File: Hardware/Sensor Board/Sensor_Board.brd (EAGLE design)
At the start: 100 x 80 mm, 19 parts, among them Q1 MOSFET-NCHANNELFQP30N06L, U1 ATMEGA328P_PDIP

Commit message: Add communications
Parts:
- added FRAME1: FRAME-LETTER, SparkFun-Aesthetics:CREATIVE_COMMONS
- added R1, R3: 120, SparkFun-Passives:1206
- added U$7: MAX3077, MAX3077:MAX3070E
- added U$8: RJ45-8PTH, SparkFun-Connectors:RJ45-8
- C1: device SparkFun-Capacitors:1206 -> SparkFun-Capacitors:CPOL-RADIAL-100UF-25V
- C5: value 100uF -> 10uF
- moved U$2 75.7 mm to (-22.9, -174.0)
- moved C1 56.2 mm to (-24.1, -100.3)
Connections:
- new net N$6: R1.1, U$7.A, U$8.1
- new net N$7: R1.2, U$7.B, U$8.2
- new net N$8: R3.1, U$7.Z, U$8.6
- new net N$9: R3.2, U$7.Y, U$8.3
- new net ROVECOMM_RX: U$7.RO, U1.2
- new net ROVECOMM_TX: U$7.DI, U1.3
- net 5V: now also U$7.VCC
- net GND: now also U$7.GND
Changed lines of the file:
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@@
 <element name="12V_INPUT" library="SparkFun-Connectors" package="MOLEX-1X2" value="M02POLAR" x="-7.62" y="-21.59"/>
 <element name="R2" library="SparkFun-Passives" package="1206" value="1k" x="-6.35" y="-35.56"/>
-<element name="C5" library="SparkFun-Capacitors" package="1206" value="100uF" x="-6.35" y="-39.37"/>
+<element name="C5" library="SparkFun-Capacitors" package="1206" value="10uF" x="-6.35" y="-39.37"/>
 <element name="C6" library="SparkFun-Capacitors" package="1206" value="10uF" x="-6.35" y="-43.18"/>
-<element name="C1" library="SparkFun-Capacitors" package="1206" value="100uF" x="-6.35" y="-46.99"/>
 <element name="LED1" library="SparkFun-LED" package="LED-1206" value="" x="-6.35" y="-52.07"/>
 <element name="U$1" library="MRDT-2015-PowerBoard" package="OKI-78SRH" value="Q_OKI-78SR" x="-15.24" y="-49.53"/>
-<element name="U$2" library="MRDT-2015-General" package="TEST" value="TEST" x="6.35" y="-104.14"/>
+<element name="C1" library="SparkFun-Capacitors" package="CPOL-RADIAL-100UF-25V" value="100uF" x="-24.13" y="-100.33"/>
+<element name="U$7" library="MAX3077" package="MAX3070E" value="MAX3077" x="-30.48" y="-100.33"/>
+<element name="U$8" library="SparkFun-Connectors" package="RJ45-8" value="RJ45-8PTH" x="-41.91" y="-93.98"/>
+<element name="R1" library="SparkFun-Passives" package="1206" value="120" x="-46.99" y="-107.95"/>
+<element name="R3" library="SparkFun-Passives" package="1206" value="120" x="-46.99" y="-111.76"/>
+<element name="FRAME1" library="SparkFun-Aesthetics" package="CREATIVE_COMMONS" value="FRAME-LETTER" x="-27.94" y="-121.92"/>
+<element name="U$2" library="MRDT-2015-General" package="TEST" value="TEST" x="-22.86" y="-173.99"/>
 </elements>
 <signals>
@@
 <contactref element="U$4" pad="GND"/>
 <contactref element="Q1" pad="3"/>
+<contactref element="U$1" pad="2"/>
 <contactref element="C1" pad="2"/>
-<contactref element="U$1" pad="2"/>
-<wire x1="33.02" y1="44.45" x2="30.61" y2="46.99" width="0" layer="19" extent="1-1"/>
+<contactref element="U$7" pad="GND"/>
+<wire x1="-25.4" y1="-100.33" x2="-28.575" y2="-103.1875" width="0" layer="19" extent="1-1"/>
+<wire x1="-15.24" y1="-49.53" x2="-25.4" y2="-100.33" width="0" layer="19" extent="1-1"/>
+<wire x1="-4.95" y1="-43.18" x2="-15.24" y2="-49.53" width="0" layer="19" extent="1-1"/>
+<wire x1="-4.95" y1="-39.37" x2="-4.95" y2="-43.18" width="0" layer="19" extent="1-1"/>
+<wire x1="-4.95" y1="-35.56" x2="-4.95" y2="-39.37" width="0" layer="19" extent="1-1"/>
+<wire x1="-7.62" y1="-21.59" x2="-4.95" y2="-35.56" width="0" layer="19" extent="1-1"/>
+<wire x1="7.62" y1="-19.05" x2="-7.62" y2="-21.59" width="0" layer="19" extent="1-1"/>
+<wire x1="5.08" y1="-10.16" x2="7.62" y2="-19.05" width="0" layer="19" extent="1-1"/>
+<wire x1="49.53" y1="10.16" x2="5.08" y2="-10.16" width="0" layer="19" extent="1-1"/>
+<wire x1="30.61" y1="46.99" x2="33.02" y2="44.45" width="0" layer="19" extent="1-1"/>
 <wire x1="21.46" y1="46.99" x2="30.61" y2="46.99" width="0" layer="19" extent="1-1"/>
-<wire x1="5.08" y1="-10.16" x2="49.53" y2="10.16" width="0" layer="19" extent="1-1"/>
-<wire x1="7.62" y1="-19.05" x2="5.08" y2="-10.16" width="0" layer="19" extent="1-1"/>
-<wire x1="-7.62" y1="-21.59" x2="7.62" y2="-19.05" width="0" layer="19" extent="1-1"/>
-<wire x1="-4.95" y1="-35.56" x2="-7.62" y2="-21.59" width="0" layer="19" extent="1-1"/>
-<wire x1="-4.95" y1="-39.37" x2="-4.95" y2="-35.56" width="0" layer="19" extent="1-1"/>
-<wire x1="-4.95" y1="-43.18" x2="-4.95" y2="-39.37" width="0" layer="19" extent="1-1"/>
-<wire x1="-4.95" y1="-46.99" x2="-4.95" y2="-43.18" width="0" layer="19" extent="1-1"/>
-<wire x1="-15.24" y1="-49.53" x2="-4.95" y2="-46.99" width="0" layer="19" extent="1-1"/>
 </signal>
 <signal name="5V">
@@
 <contactref element="U$4" pad="VCC"/>
 <contactref element="LED1" pad="A"/>
+<contactref element="U$7" pad="VCC"/>
+<wire x1="-7.85" y1="-52.07" x2="-32.385" y2="-103.1875" width="0" layer="19" extent="1-1"/>
 <wire x1="-7.75" y1="-43.18" x2="-7.85" y2="-52.07" width="0" layer="19" extent="1-1"/>
 <wire x1="10.16" y1="-19.05" x2="-7.75" y2="-43.18" width="0" layer="19" extent="1-1"/>
@@
 <signal name="3V3_LASER">
 <contactref element="JP3" pad="2"/>
+<contactref element="U$1" pad="3"/>
 <contactref element="C1" pad="1"/>
-<contactref element="U$1" pad="3"/>
-<wire x1="-7.75" y1="-46.99" x2="-17.78" y2="-49.53" width="0" layer="19" extent="1-1"/>
-<wire x1="13.97" y1="49.53" x2="-7.75" y2="-46.99" width="0" layer="19" extent="1-1"/>
+<wire x1="-17.78" y1="-49.53" x2="-22.86" y2="-100.33" width="0" layer="19" extent="1-1"/>
+<wire x1="13.97" y1="49.53" x2="-17.78" y2="-49.53" width="0" layer="19" extent="1-1"/>
 </signal>
 <signal name="N$2">
@@
 <wire x1="-7.75" y1="-35.56" x2="-4.85" y2="-52.07" width="0" layer="19" extent="1-1"/>
 </signal>
+<signal name="N$6">
+<contactref element="U$7" pad="A"/>
+<contactref element="R1" pad="1"/>
+<contactref element="U$8" pad="1"/>
+<wire x1="-32.385" y1="-97.4725" x2="-48.39" y2="-107.95" width="0" layer="19" extent="1-1"/>
+<wire x1="-46.355" y1="-87.63" x2="-32.385" y2="-97.4725" width="0" layer="19" extent="1-1"/>
+</signal>
+<signal name="N$7">
+<contactref element="U$7" pad="B"/>
+<contactref element="U$8" pad="2"/>
+<contactref element="R1" pad="2"/>
+<wire x1="-31.115" y1="-97.4725" x2="-45.59" y2="-107.95" width="0" layer="19" extent="1-1"/>
+<wire x1="-45.085" y1="-85.09" x2="-31.115" y2="-97.4725" width="0" layer="19" extent="1-1"/>
+</signal>
+<signal name="N$8">
+<contactref element="U$7" pad="Z"/>
+<contactref element="U$8" pad="6"/>
+<contactref element="R3" pad="1"/>
+<wire x1="-29.845" y1="-97.4725" x2="-48.39" y2="-111.76" width="0" layer="19" extent="1-1"/>
+<wire x1="-40.005" y1="-85.09" x2="-29.845" y2="-97.4725" width="0" layer="19" extent="1-1"/>
+</signal>
+<signal name="N$9">
+<contactref element="U$7" pad="Y"/>
+<contactref element="U$8" pad="3"/>
+<contactref element="R3" pad="2"/>
+<wire x1="-28.575" y1="-97.4725" x2="-45.59" y2="-111.76" width="0" layer="19" extent="1-1"/>
+<wire x1="-43.815" y1="-87.63" x2="-28.575" y2="-97.4725" width="0" layer="19" extent="1-1"/>
+</signal>
+<signal name="ROVECOMM_TX">
+<contactref element="U1" pad="3"/>
+<contactref element="U$7" pad="DI"/>
+<wire x1="45.72" y1="44.45" x2="-29.845" y2="-103.1875" width="0" layer="19" extent="1-1"/>
+</signal>
+<signal name="ROVECOMM_RX">
+<contactref element="U1" pad="2"/>
+<contactref element="U$7" pad="RO"/>
+<wire x1="48.26" y1="44.45" x2="-31.115" y2="-103.1875" width="0" layer="19" extent="1-1"/>
+</signal>
 </signals>

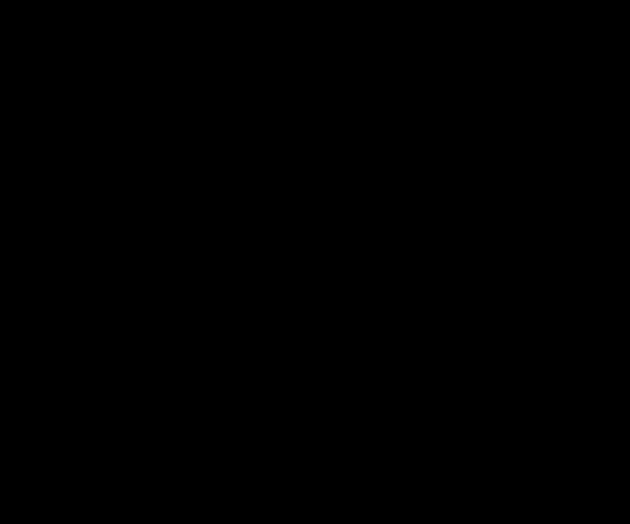
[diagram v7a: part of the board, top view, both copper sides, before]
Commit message: #2 Add reset button to microcontroller
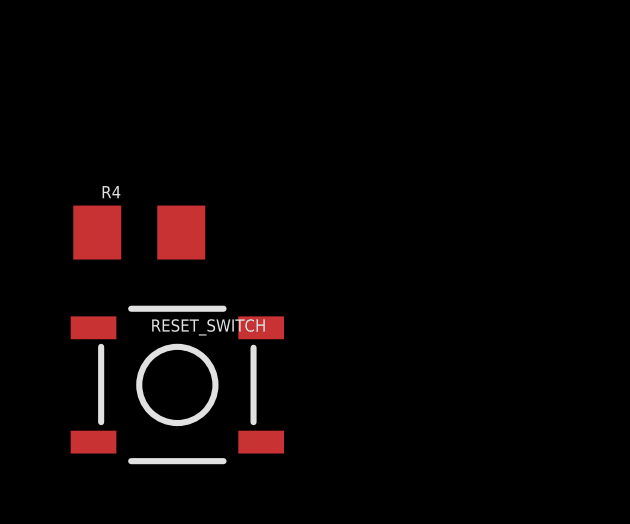
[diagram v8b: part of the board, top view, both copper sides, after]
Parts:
- added R4: 10k, SparkFun-Passives:1206
- added RESET_SWITCH: SWITCH-MOMENTARY-2SMD, SparkFun-Electromechanical:TACTILE-SWITCH-SMD
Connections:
- new net N$10: R4.2, RESET_SWITCH.1, U1.1
- net 3.3V: now also R4.1
- net GND: now also C3.1, C4.1, RESET_SWITCH.3; no longer C3.2, C4.2
- net N$2: now also C4.2; no longer C3.1
- net N$4: now also C3.2; no longer C4.1
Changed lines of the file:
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@@
 <?xml version="1.0" encoding="utf-8"?>
 <!DOCTYPE eagle SYSTEM "eagle.dtd">
-<eagle version="6.5.0">
+<eagle version="7.2.0">
 <drawing>
 <settings>
@@
 <layer number="59" name="tCarbon" color="7" fill="1" visible="no" active="no"/>
 <layer number="60" name="bCarbon" color="7" fill="1" visible="no" active="no"/>
-<layer number="90" name="Modules" color="5" fill="1" visible="yes" active="yes"/>
+<layer number="90" name="Modules" color="5" fill="1" visible="no" active="no"/>
 <layer number="91" name="Nets" color="2" fill="1" visible="no" active="no"/>
 <layer number="92" name="Busses" color="1" fill="1" visible="no" active="no"/>
@@
 <pass name="Default">
 <param name="RoutingGrid" value="50mil"/>
+<param name="AutoGrid" value="1"/>
+<param name="Efforts" value="0"/>
+<param name="TopRouterVariant" value="1"/>
 <param name="tpViaShape" value="round"/>
 <param name="PrefDir.1" value="|"/>
@@
 <element name="FRAME1" library="SparkFun-Aesthetics" package="CREATIVE_COMMONS" value="FRAME-LETTER" x="-27.94" y="-121.92"/>
 <element name="U$2" library="MRDT-2015-General" package="TEST" value="TEST" x="-22.86" y="-173.99"/>
+<element name="R4" library="SparkFun-Passives" package="1206" value="10k" x="-46.99" y="-182.88"/>
+<element name="RESET_SWITCH" library="SparkFun-Electromechanical" package="TACTILE-SWITCH-SMD" value="SWITCH-MOMENTARY-2SMD" x="-45.72" y="-187.96">
+<attribute name="PROD_ID" value="SWCH-08247" x="-45.72" y="-187.96" size="1.778" layer="27" display="off"/>
+</element>
 </elements>
 <signals>
 <signal name="GND">
 <contactref element="U$3" pad="GND"/>
-<contactref element="U1" pad="22"/>
-<contactref element="U1" pad="8"/>
 <contactref element="U$5" pad="GND"/>
 <polygon width="0.4064" layer="16">
@@
 <vertex x="-2.54" y="-3.81"/>
 </polygon>
-<contactref element="C4" pad="2"/>
-<contactref element="C3" pad="2"/>
 <contactref element="U$6" pad="GND"/>
 <contactref element="LM7805" pad="GND"/>
@@
 <contactref element="C1" pad="2"/>
 <contactref element="U$7" pad="GND"/>
+<contactref element="U1" pad="22"/>
+<contactref element="U1" pad="8"/>
+<contactref element="C3" pad="1"/>
+<contactref element="C4" pad="1"/>
+<contactref element="RESET_SWITCH" pad="3"/>
+<wire x1="-28.575" y1="-103.1875" x2="-48.514" y2="-189.865" width="0" layer="19" extent="1-1"/>
 <wire x1="-25.4" y1="-100.33" x2="-28.575" y2="-103.1875" width="0" layer="19" extent="1-1"/>
 <wire x1="-15.24" y1="-49.53" x2="-25.4" y2="-100.33" width="0" layer="19" extent="1-1"/>
@@
 <wire x1="5.08" y1="-10.16" x2="7.62" y2="-19.05" width="0" layer="19" extent="1-1"/>
 <wire x1="49.53" y1="10.16" x2="5.08" y2="-10.16" width="0" layer="19" extent="1-1"/>
-<wire x1="30.61" y1="46.99" x2="33.02" y2="44.45" width="0" layer="19" extent="1-1"/>
-<wire x1="21.46" y1="46.99" x2="30.61" y2="46.99" width="0" layer="19" extent="1-1"/>
+<wire x1="49.53" y1="15.24" x2="49.53" y2="10.16" width="0" layer="19" extent="1-1"/>
+<wire x1="44.45" y1="33.02" x2="49.53" y2="15.24" width="0" layer="19" extent="1-1"/>
+<wire x1="35.56" y1="36.83" x2="44.45" y2="33.02" width="0" layer="19" extent="1-1"/>
+<wire x1="33.02" y1="33.02" x2="35.56" y2="36.83" width="0" layer="19" extent="1-1"/>
+<wire x1="33.02" y1="44.45" x2="35.56" y2="36.83" width="0" layer="19" extent="1-1"/>
+<wire x1="34.29" y1="48.26" x2="33.02" y2="44.45" width="0" layer="19" extent="1-1"/>
+<wire x1="27.81" y1="46.99" x2="33.02" y2="44.45" width="0" layer="19" extent="1-1"/>
+<wire x1="24.26" y1="46.99" x2="27.81" y2="46.99" width="0" layer="19" extent="1-1"/>
 </signal>
 <signal name="5V">
@@
 <contactref element="U1" pad="21"/>
 <contactref element="U1" pad="20"/>
-<wire x1="33.02" y1="36.83" x2="35.56" y2="44.45" width="0" layer="19" extent="1-1"/>
-<wire x1="30.48" y1="36.83" x2="33.02" y2="36.83" width="0" layer="19" extent="1-1"/>
+<contactref element="R4" pad="1"/>
+<wire x1="30.48" y1="36.83" x2="-48.39" y2="-182.88" width="0" layer="19" extent="1-1"/>
+<wire x1="33.02" y1="36.83" x2="30.48" y2="36.83" width="0" layer="19" extent="1-1"/>
+<wire x1="35.56" y1="44.45" x2="33.02" y2="36.83" width="0" layer="19" extent="1-1"/>
 </signal>
 <signal name="N$5">
@@
 <contactref element="U$4" pad="PRB"/>
 <wire x1="46.99" y1="10.16" x2="46.99" y2="15.24" width="0" layer="19" extent="1-1"/>
-</signal>
-<signal name="N$4">
-<contactref element="U1" pad="10"/>
-<contactref element="16MHZ" pad="1"/>
-<contactref element="C4" pad="1"/>
-<wire x1="24.26" y1="46.99" x2="22.86" y2="50.8" width="0" layer="19" extent="1-1"/>
-<wire x1="27.94" y1="44.45" x2="24.26" y2="46.99" width="0" layer="19" extent="1-1"/>
 </signal>
 <signal name="MOIS_SENSOR">
@@
 <wire x1="-17.78" y1="-49.53" x2="-22.86" y2="-100.33" width="0" layer="19" extent="1-1"/>
 <wire x1="13.97" y1="49.53" x2="-17.78" y2="-49.53" width="0" layer="19" extent="1-1"/>
-</signal>
-<signal name="N$2">
-<contactref element="16MHZ" pad="2"/>
-<contactref element="C3" pad="1"/>
-<contactref element="U1" pad="9"/>
-<wire x1="27.81" y1="46.99" x2="27.94" y2="50.8" width="0" layer="19" extent="1-1"/>
-<wire x1="30.48" y1="44.45" x2="27.81" y2="46.99" width="0" layer="19" extent="1-1"/>
 </signal>
 <signal name="N$1">
@@
 <wire x1="48.26" y1="44.45" x2="-31.115" y2="-103.1875" width="0" layer="19" extent="1-1"/>
 </signal>
+<signal name="N$10">
+<contactref element="U1" pad="1"/>
+<contactref element="R4" pad="2"/>
+<contactref element="RESET_SWITCH" pad="1"/>
+<wire x1="-45.59" y1="-182.88" x2="-48.514" y2="-186.055" width="0" layer="19" extent="1-1"/>
+<wire x1="50.8" y1="44.45" x2="-45.59" y2="-182.88" width="0" layer="19" extent="1-1"/>
+</signal>
+<signal name="N$2">
+<contactref element="C4" pad="2"/>
+<contactref element="16MHZ" pad="2"/>
+<contactref element="U1" pad="9"/>
+<wire x1="30.48" y1="44.45" x2="27.94" y2="50.8" width="0" layer="19" extent="1-1"/>
+<wire x1="21.46" y1="46.99" x2="27.94" y2="50.8" width="0" layer="19" extent="1-1"/>
+</signal>
+<signal name="N$4">
+<contactref element="C3" pad="2"/>
+<contactref element="16MHZ" pad="1"/>
+<contactref element="U1" pad="10"/>
+<wire x1="27.94" y1="44.45" x2="30.61" y2="46.99" width="0" layer="19" extent="1-1"/>
+<wire x1="22.86" y1="50.8" x2="27.94" y2="44.45" width="0" layer="19" extent="1-1"/>
+</signal>
 </signals>
